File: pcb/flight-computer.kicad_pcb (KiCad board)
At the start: 4 copper layers, 83.7 x 62.9 mm, 90 parts, among them J1 MicroSD Slot, J2 USB_C_Receptacle_USB2.0_16P, J3 SMA_Coax, J4 Conn_01x02, J5 ARM, Q1 PMOS, U1 RP2040, U10 LM3671MF, U11 TPS2116DRL, U2 W25Q16JVSS, U3 USBLC6-2SC6, U4 M24C32-FMN, U5 MS5607-02BA, U6 LIS2MDL, U7 LSM6DSO32TR, U8 LC86G, U9 RN2903, Y1 12MHz

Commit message: Teardrops and some cleanup
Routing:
- net GND: track 297.5 -> 300.3 mm
- net MCU_UART1_TX: track 39.6 -> 40.2 mm

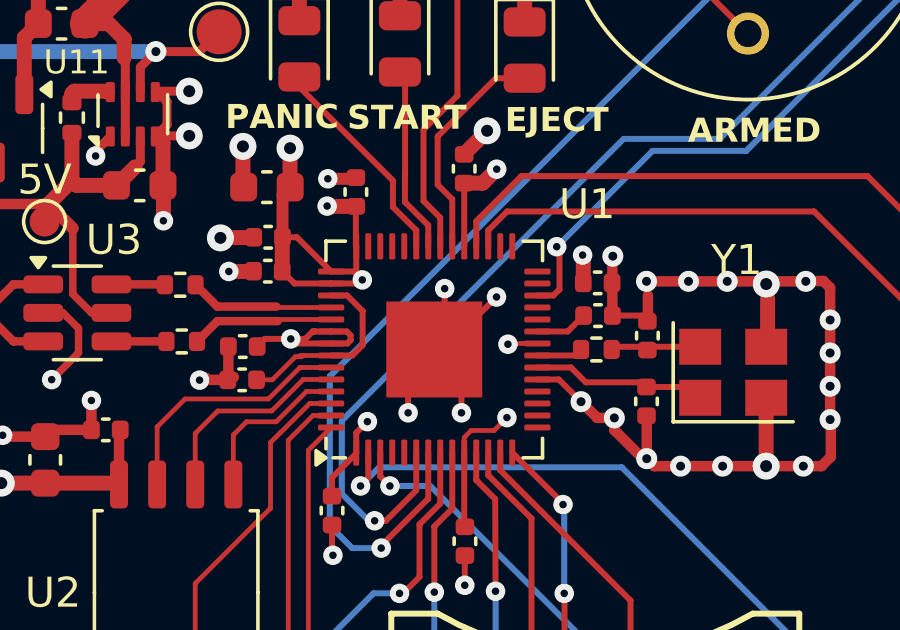
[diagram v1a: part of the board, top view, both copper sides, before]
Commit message: Fixed disconnected 1V1 rails
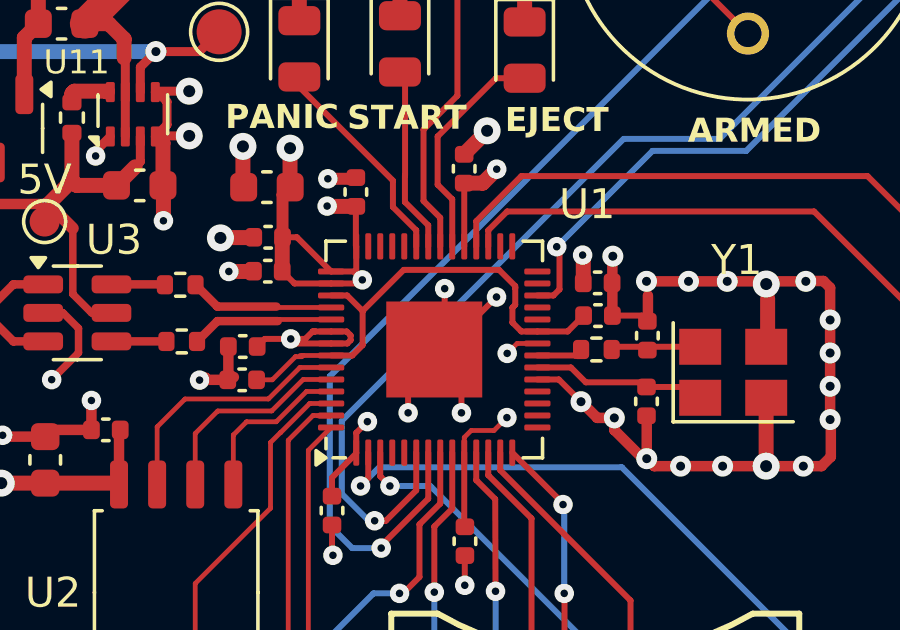
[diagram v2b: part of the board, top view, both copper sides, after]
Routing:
- net +1V1: track 8.27 -> 16.4 mm

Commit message: Added battery charge monitor
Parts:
- removed REF**: OSHW-Logo_7.5x8mm_SilkScreen, Symbol:OSHW-Logo_7.5x8mm_SilkScreen
- added R21: 10k, Resistor_SMD:R_0402_1005Metric, F.Cu at (90.3, 80.3)
- added R22: 33k, Resistor_SMD:R_0402_1005Metric, F.Cu at (90.8, 82.1)
- added R23: 330R, Resistor_SMD:R_0402_1005Metric, F.Cu at (90.8, 84.5)
- R1, R16: value 11k -> 10k
- renumbered BOOT to SW1, RST to SW2, GND to TP1, PWR to TP2, 5V to TP3, 3V3 to TP4, 3V7 to TP5, BAT to TP6
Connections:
- U1 pad 38: unconnected-(U1-GPIO26_ADC0-Pad38) -> ADC0
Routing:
- net ADC0: track 0.00 -> 29.9 mm, vias 0 -> 2
- net /Power/BAT+: track 14.9 -> 18.7 mm
- net Net-(R22-Pad2): track 0.00 -> 1.33 mm
- net GND: track 300.3 -> 301.5 mm, vias 85 -> 86
- net /PANIC: track 7.26 -> 7.78 mm

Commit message: Added interrupt lines for IMU and magnetometer
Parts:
- added REF**: OSHW-Logo_7.5x8mm_SilkScreen, Symbol:OSHW-Logo_7.5x8mm_SilkScreen, F.Cu at (162.0, 120.4)
- renumbered TP4 to 3V3, TP5 to 3V7, TP3 to 5V, TP6 to BAT, TP1 to GND, TP2 to PWR
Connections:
- U1 pad 15: unconnected-(U1-GPIO12-Pad15) -> MAG_INT
- U1 pad 16: unconnected-(U1-GPIO13-Pad16) -> GYRO_INT
- U1 pad 17: unconnected-(U1-GPIO14-Pad17) -> XL_INT
- U6 pad 7: unconnected-(U6-DRDY-Pad7) -> MAG_INT
- U7 pad 4: unconnected-(U7-INT1-Pad4) -> GYRO_INT
- U7 pad 9: unconnected-(U7-INT2-Pad9) -> XL_INT
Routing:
- net MAG_INT: track 0.00 -> 57.7 mm, vias 0 -> 2
- net XL_INT: track 0.00 -> 46.2 mm, vias 0 -> 2
- net GYRO_INT: track 0.00 -> 45.9 mm, vias 0 -> 2
- net I2C0_SCL: track 72.8 -> 74.4 mm

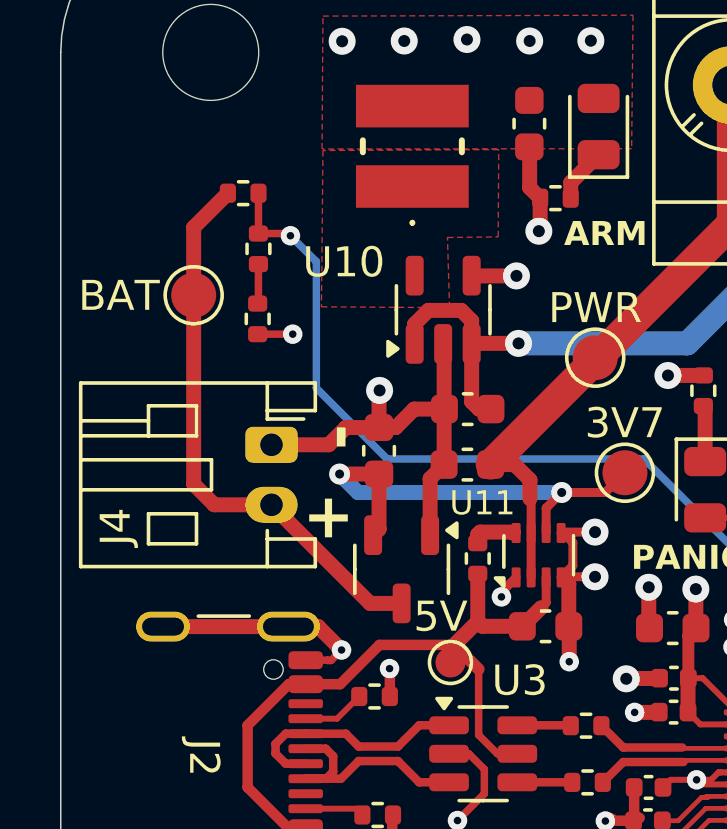
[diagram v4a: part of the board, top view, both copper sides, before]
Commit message: Battery charge detection after reverse polarity protection for safety.
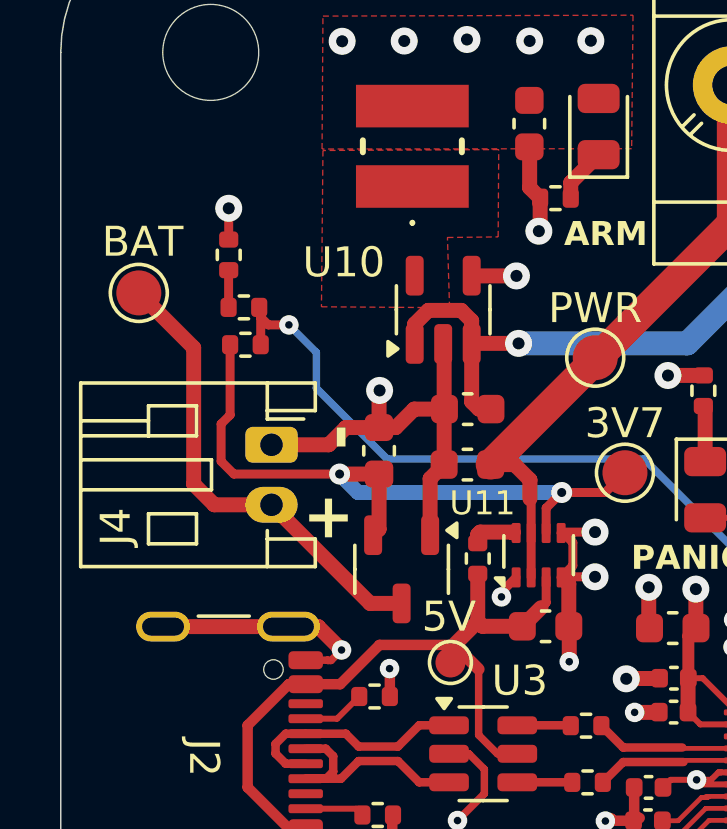
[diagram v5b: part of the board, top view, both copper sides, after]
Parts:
- moved R21 5.05 mm to (90.3, 85.3)
- moved R23 2.34 mm to (89.8, 82.3), turned to 90 degrees
- moved R22 2.01 mm to (90.3, 84.1), turned to 180 degrees
- moved BAT 1.83 mm to (86.8, 83.6)
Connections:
- R21 pad 2: /Power/BAT+ -> +3V7
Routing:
- net +3V7: track 15.0 -> 23.2 mm
- net ADC0: track 29.9 -> 26.6 mm
- net /Power/BAT+: track 18.7 -> 15.7 mm

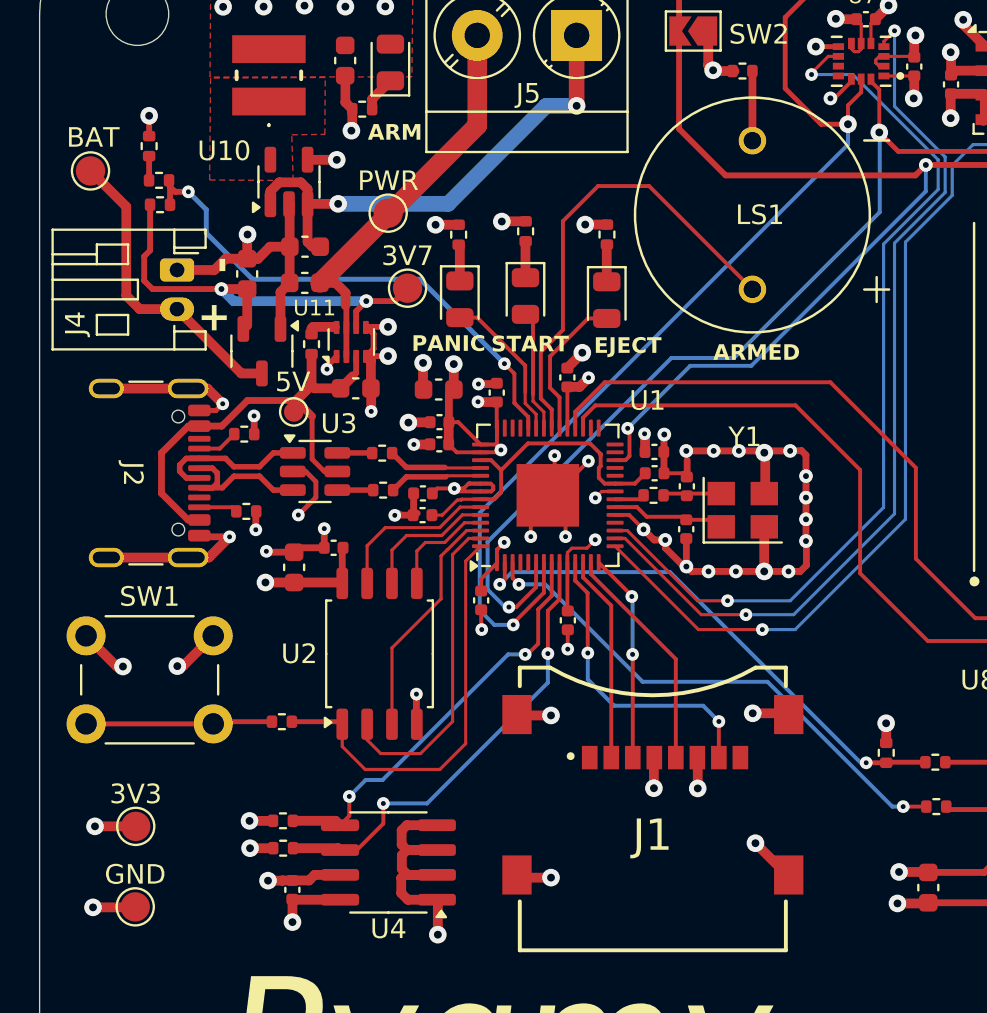
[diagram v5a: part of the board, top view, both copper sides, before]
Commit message: Revamping docs, added SWD test pads.
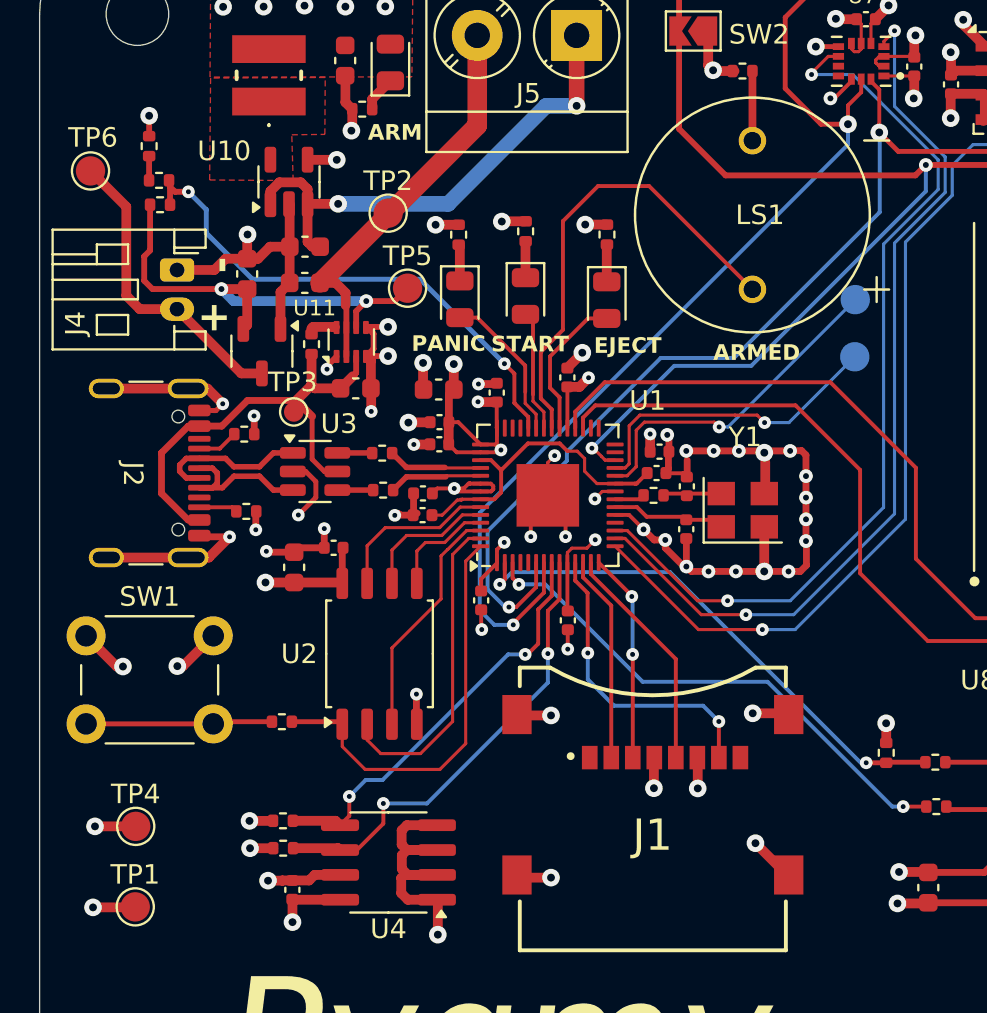
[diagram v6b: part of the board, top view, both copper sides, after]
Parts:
- added TP7: TestPoint, TestPoint:TestPoint_Pad_D1.5mm, B.Cu at (125.9, 90.2)
- added TP8: TestPoint, TestPoint:TestPoint_Pad_D1.5mm, B.Cu at (125.9, 93.1)
- moved C10 0.26 mm to (115.9, 98.0)
- moved C5 0.10 mm to (115.7, 99.1)
- renumbered GND to TP1, PWR to TP2, 5V to TP3, 3V3 to TP4, 3V7 to TP5, BAT to TP6
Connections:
- U1 pad 24: unconnected-(U1-SWCLK-Pad24) -> Net-(U1-SWCLK)
- U1 pad 25: unconnected-(U1-SWD-Pad25) -> Net-(U1-SWD)
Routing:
- net Net-(U1-SWCLK): track 0.00 -> 17.3 mm, vias 0 -> 1
- net Net-(U1-SWD): track 0.00 -> 16.1 mm, vias 0 -> 1
- net GND: track 301.4 -> 299.2 mm, vias 86 -> 85
- net RST_N: track 75.6 -> 77.0 mm
- net I2C0_SDA: track 62.4 -> 63.0 mm

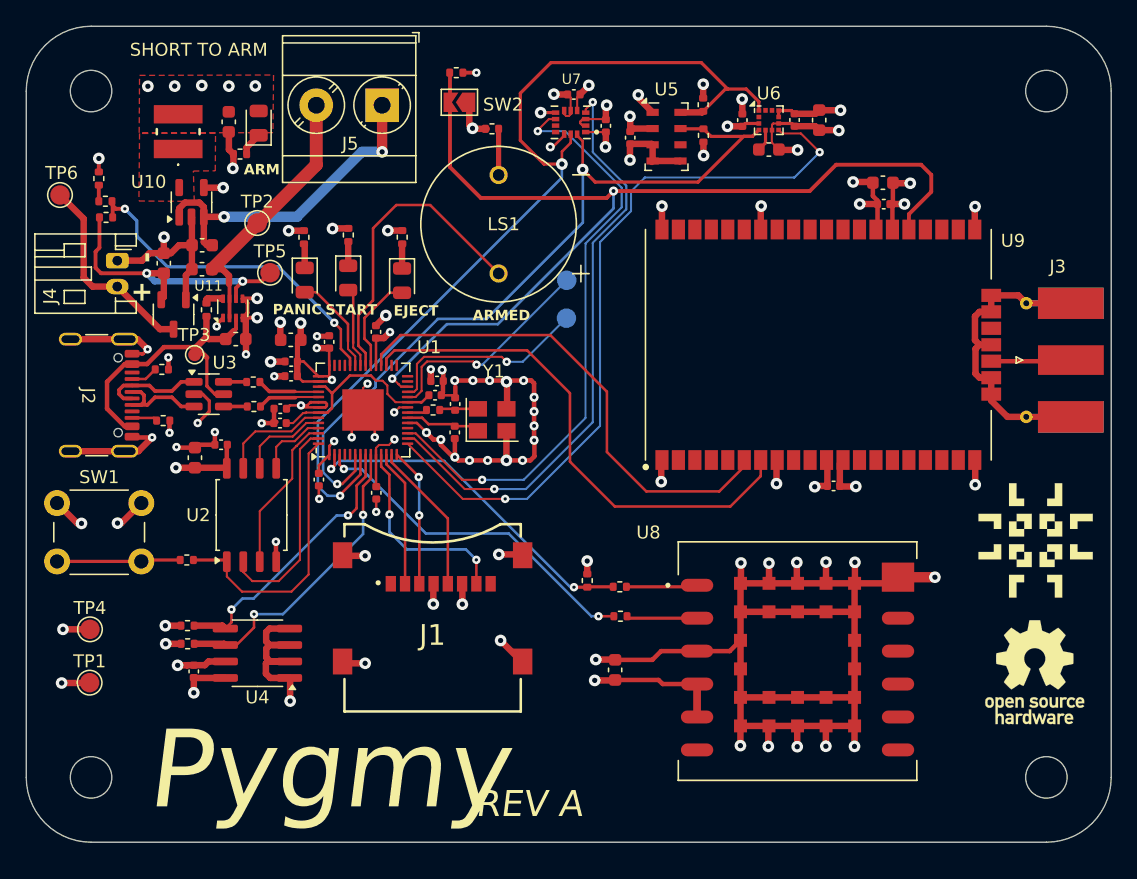
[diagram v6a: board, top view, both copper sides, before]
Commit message: Added MOSFET to drive the buzzer.
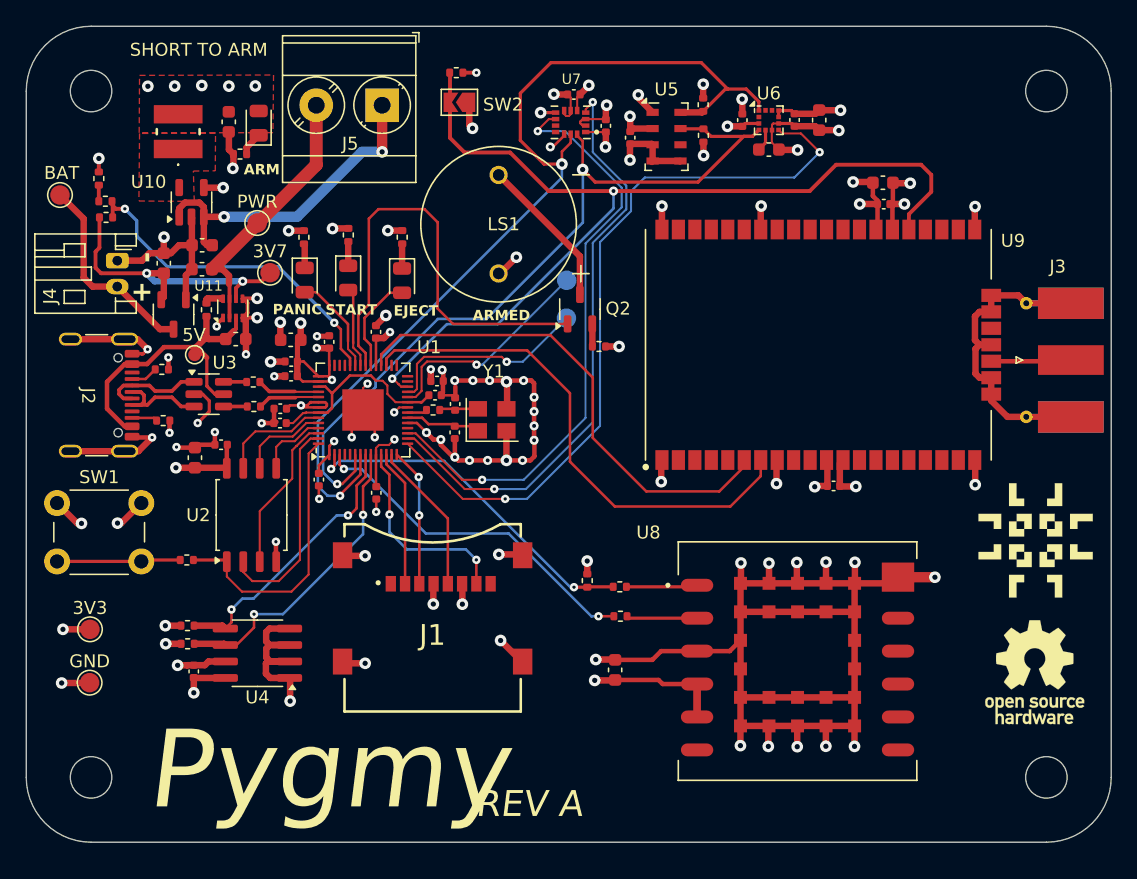
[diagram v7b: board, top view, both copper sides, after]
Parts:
- added Q2: NMOS, Package_TO_SOT_SMD:SOT-23-3, F.Cu at (126.9, 92.4)
- R12: value 100R -> 330R
- R13, R14, R17: value 68R -> 330R
- moved R15 18.7 mm to (128.4, 95.3), turned to 0 degrees
- renumbered TP4 to 3V3, TP5 to 3V7, TP3 to 5V, TP6 to BAT, TP1 to GND, TP2 to PWR, TP7 to SWCLK, TP8 to SWD
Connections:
- LS1 pad N: Net-(LS1-PadN) -> Net-(Q2-D)
- LS1 pad P: /BUZZ -> +3V3
- R15 pad 1: Net-(LS1-PadN) -> Net-(Q2-S)
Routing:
- net Net-(Q2-D): track 0.00 -> 11.8 mm
- net /BUZZ: track 23.9 -> 35.1 mm
- net Net-(LS1-PadN): track 3.56 -> 0.00 mm
- net +3V3: track 94.0 -> 95.9 mm, vias 36 -> 37
- net RST_N: track 77.0 -> 75.3 mm
- net Net-(Q2-S): track 0.00 -> 1.74 mm
- net GND: vias 85 -> 86
